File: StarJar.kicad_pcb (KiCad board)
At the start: 2 copper layers, 127 x 50.8 mm, 38 parts, among them J1 USB_A, J2 GM_Tube, J3 Screw_Terminal_1x02, Q1 JN3303, Q2 2N3904, Q3 2N3904, Q4 2N3904, U1 LM555N, U2 LMV321

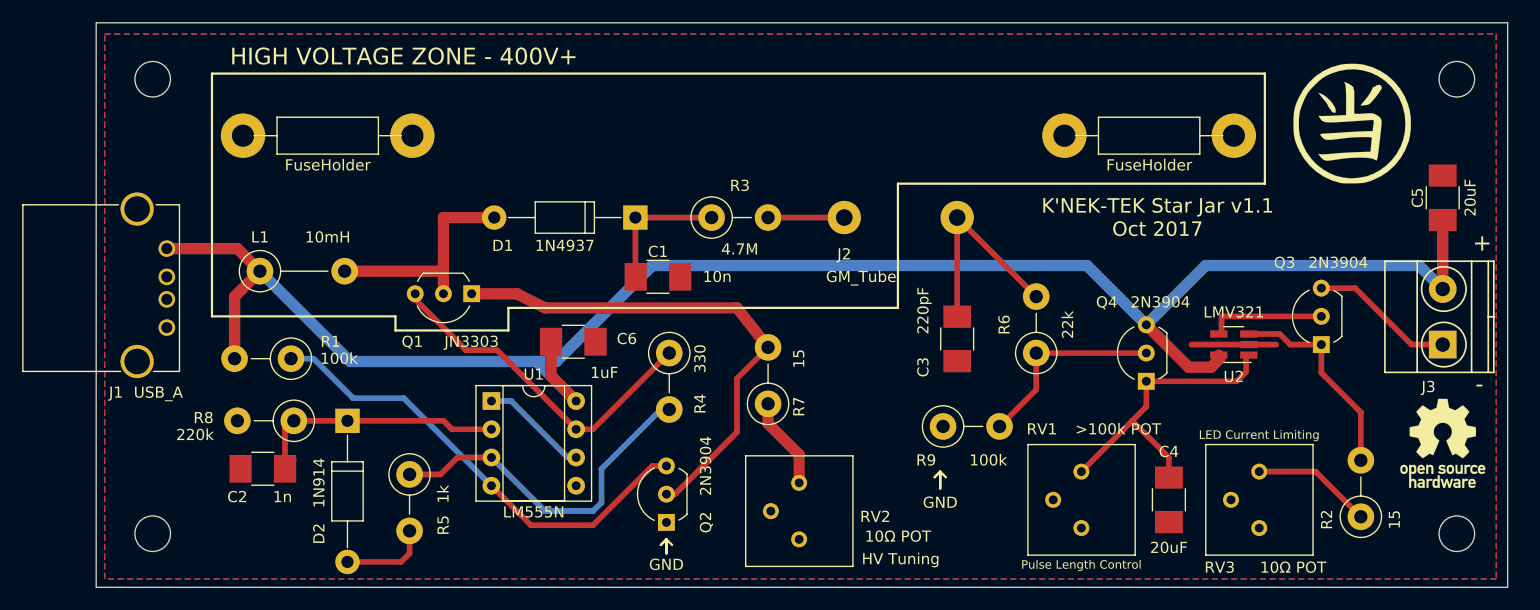
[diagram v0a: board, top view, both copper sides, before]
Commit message: Add files via upload
v1.2 board layout finished, ready to order. Changes: zip tie mounts for GM tube, USB micro-B rather than USB-A, added new components to fix pulse size issue.
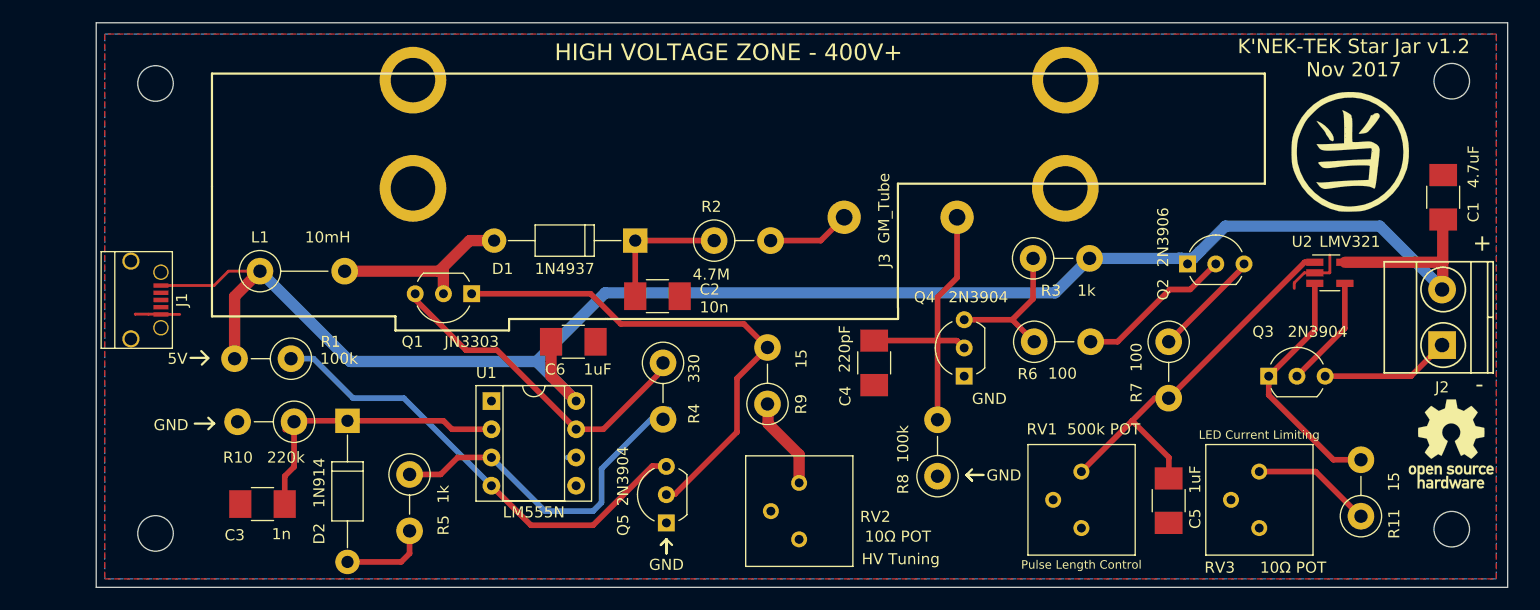
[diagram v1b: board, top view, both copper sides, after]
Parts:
- removed the FuseHolder1 at (149.4, 64.8)
- removed the FuseHolder1 at (75.4, 64.8)
- removed the REF** at (184.7, 59.7)
- removed the REF** at (184.7, 100.6)
- removed the REF** at (67.3, 100.6)
- removed the REF** at (67.3, 59.7)
- added FuseHolder1: ZipTie, CustomFootprints:GM_tube_ziptie_mounts, F.Cu at (90.7, 69.5)
- added FuseHolder1: ZipTie, CustomFootprints:GM_tube_ziptie_mounts, F.Cu at (149.4, 69.5)
- added Q5: 2N3904, TO_SOT_Packages_THT:TO-92_Inline_Wide, F.Cu at (113.5, 99.6)
- added R10: 220k, Resistors_THT:R_Axial_DIN0411_L9.9mm_D3.6mm_P5.08mm_Vertical, F.Cu at (80.0, 90.5)
- added R11: 15, Resistors_THT:R_Axial_DIN0411_L9.9mm_D3.6mm_P5.08mm_Vertical, F.Cu at (176.0, 99.0)
- added REF**: MountingHole_3.2mm_M3, Mounting_Holes:MountingHole_3.2mm_M3, F.Cu at (184.2, 100.2)
- added REF**: MountingHole_3.2mm_M3, Mounting_Holes:MountingHole_3.2mm_M3, F.Cu at (184.2, 59.9)
- added REF**: MountingHole_3.2mm_M3, Mounting_Holes:MountingHole_3.2mm_M3, F.Cu at (67.6, 100.6)
- added REF**: MountingHole_3.2mm_M3, Mounting_Holes:MountingHole_3.2mm_M3, F.Cu at (67.6, 60.1)
- C1: value 10n -> 4.7uF
- C2: value 1n -> 10n
- C3: value 220pF -> 1n
- C4: value 20uF -> 220pF
- C5: value 20uF -> 1uF
- J1: value USB_A -> USB_OTG; footprint Connectors:USB_A -> CustomFootprints:USB_Micro-B_big_holes_for_OSHpark
- J2: value GM_Tube -> Screw_Terminal_1x02; footprint Wire_Connections_Bridges:WireConnection_1.50mmDrill -> Connectors_Terminal_Blocks:TerminalBlock_Pheonix_MKDS1.5-2pol
- J3: value Screw_Terminal_1x02 -> GM_Tube; footprint Connectors_Terminal_Blocks:TerminalBlock_Pheonix_MKDS1.5-2pol -> Wire_Connections_Bridges:WireConnection_1.50mmDrill
- Q2: value 2N3904 -> 2N3906
- R2: value 15 -> 4.7M
- R3: value 4.7M -> 1k
- R6: value 22k -> 100
- R7: value 15 -> 100
- R8: value 220k -> 100k
- R9: value 100k -> 15
- RV1: value >100k POT -> 500k POT
- moved C1 71.0 mm to (183.4, 70.3), turned to 90 degrees
- moved C3 64.3 mm to (77.2, 97.9), turned to 180 degrees
- moved R2 63.3 mm to (117.8, 74.2), turned to 0 degrees
- moved R8 58.1 mm to (137.9, 95.4), turned to 90 degrees
- moved J3 55.1 mm to (129.5, 72.1), turned to 0 degrees
- moved J2 55.0 mm to (183.3, 83.6), turned to 90 degrees
- moved Q2 52.3 mm to (160.4, 76.3), turned to 0 degrees
- moved C2 38.8 mm to (112.7, 79.2), turned to 0 degrees
- moved C5 36.8 mm to (158.7, 97.6), turned to 270 degrees
- moved R7 36.5 mm to (158.7, 83.3), turned to 270 degrees
- moved C4 29.2 mm to (132.2, 85.2)
- moved R3 29.2 mm to (146.5, 75.8)
- moved Q4 16.4 mm to (140.3, 86.4)
- moved R9 15.9 mm to (122.6, 88.9), turned to 90 degrees
- moved U2 10.8 mm to (173.2, 77.1), turned to 0 degrees
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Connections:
- C1 pad 1: Net-(C1-Pad1) -> +5V
- C4 pad 1: /PulseOutput -> Net-(C4-Pad1)
- C5 pad 1: +5V -> /PulseOutput
- D1 pad 1: Net-(C1-Pad1) -> Net-(C2-Pad1)
- D2 pad 1: Net-(C2-Pad1) -> Net-(C3-Pad1)
- J1 pad 2: Net-(J1-Pad2) -> (no net)
- J1 pad 3: Net-(J1-Pad3) -> (no net)
- J1 pad 4: GND -> (no net)
- J2 pad 2: Net-(C3-Pad1) -> +5V
- J3 pad 2: +5V -> Net-(C4-Pad1)
- Q2 pad 1: GND -> +5V
- Q2 pad 2: Net-(Q1-Pad1) -> Net-(Q2-Pad2)
- Q3 pad 3: Net-(J3-Pad1) -> Net-(J2-Pad1)
- Q4 pad 1: /PulseOutput -> GND
- Q4 pad 2: Net-(Q4-Pad2) -> Net-(C4-Pad1)
- Q4 pad 3: +5V -> Net-(Q4-Pad3)
- R1 pad 1: Net-(Q2-Pad3) -> Net-(Q5-Pad3)
- R2 pad 1: Net-(R2-Pad1) -> Net-(C2-Pad1)
- R2 pad 2: Net-(Q3-Pad1) -> Net-(J3-Pad1)
- R3 pad 1: Net-(C1-Pad1) -> Net-(Q4-Pad3)
- R3 pad 2: Net-(J2-Pad1) -> +5V
- R6 pad 1: Net-(Q4-Pad2) -> Net-(Q4-Pad3)
- R6 pad 2: Net-(C3-Pad1) -> Net-(Q2-Pad2)
- R7 pad 1: Net-(R7-Pad1) -> Net-(Q2-Pad3)
- R7 pad 2: Net-(Q1-Pad1) -> /PulseOutput
- R8 pad 1: Net-(C2-Pad1) -> GND
- R8 pad 2: GND -> Net-(C4-Pad1)
- R9 pad 1: GND -> Net-(R9-Pad1)
- R9 pad 2: Net-(Q4-Pad2) -> Net-(Q1-Pad1)
- RV1 pad 3: Net-(RV1-Pad3) -> (no net)
- RV2 pad 1: Net-(R7-Pad1) -> Net-(R9-Pad1)
- RV2 pad 3: Net-(RV2-Pad3) -> (no net)
- RV3 pad 1: Net-(R2-Pad1) -> Net-(R11-Pad1)
- RV3 pad 3: Net-(RV3-Pad3) -> (no net)
- U1 pad 2: Net-(C2-Pad1) -> Net-(C3-Pad1)
- U1 pad 4: Net-(Q2-Pad3) -> Net-(Q5-Pad3)
- U1 pad 5: Net-(U1-Pad5) -> (no net)
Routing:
- net Net-(Q5-Pad3): track 0.00 -> 42.2 mm
- net Net-(Q2-Pad3): track 42.2 -> 9.81 mm
- net Net-(C4-Pad1): track 0.00 -> 27.3 mm
- net Net-(Q4-Pad2): track 17.9 -> 0.00 mm
- net Net-(Q2-Pad2): track 0.00 -> 14.2 mm
- net Net-(Q4-Pad3): track 0.00 -> 13.4 mm
- net Net-(C1-Pad1): track 12.7 -> 0.00 mm
- net Net-(C2-Pad1): track 23.9 -> 12.1 mm
- net Net-(R2-Pad1): track 10.8 -> 0.00 mm
- net Net-(R11-Pad1): track 0.00 -> 10.8 mm
- net Net-(R9-Pad1): track 0.00 -> 8.27 mm
- net Net-(R7-Pad1): track 8.27 -> 0.00 mm
- net Net-(C3-Pad1): track 19.0 -> 27.0 mm
- net /PulseOutput: track 27.9 -> 35.3 mm
- net GND: track 17.3 -> 10.6 mm
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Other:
- board text added: "1.2"
- board text added: "5V"
- board text added: "Design files available at: https://github.com/Erik-k/StarJar"
- board text added: "K'NEK-TEK Star Jar v1.2 Nov 2017"
- board text removed: "1.1"
- board text removed: "K'NEK-TEK Star Jar v1.1 Oct 2017"

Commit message: Add files via upload
Minor changes to PCB silkscreen. Ordered the boards.
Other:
- board text added: "November 2017"
- board text removed: "1.0"
- board text removed: "September 2017"
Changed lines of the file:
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@@
-(kicad_pcb (version 4) (host pcbnew 4.0.6)
+(kicad_pcb (version 4) (host pcbnew 4.0.7)
   (general
     (links 62)
     (no_connects 0)
-    (area 62.179999 54.559999 189.280001 105.460001)
+    (area 57.952857 54.559999 255.277714 200.486)
     (thickness 1.6)
-    (drawings 61)
+    (drawings 60)
     (tracks 132)
     (zones 0)
@@
     (45 Margin user)
     (47 F.CrtYd user)
-    (49 F.Fab user hide)
+    (49 F.Fab user)
   )
   (setup
@@
     (descr "D, DO-41_SOD81 series, Axial, Horizontal, pin pitch=12.7mm, , length*diameter=5.2*2.7mm^2, , http://www.diodes.com/_files/packages/DO-41%20(Plastic).pdf")
     (tags "D DO-41_SOD81 series Axial Horizontal pin pitch 12.7mm  length 5.2mm diameter 2.7mm")
-    (fp_text reference D1 (at 11.938 -2.54 180) (layer F.SilkS)
-      (effects (font (size 1 1) (thickness 0.15)))
-    )
-    (fp_text value 1N4937 (at 6.35 -2.54 180) (layer F.SilkS)
+    (fp_text reference D1 (at 9.1046 -2.5742 180) (layer F.SilkS)
+      (effects (font (size 1 1) (thickness 0.15)))
+    )
+    (fp_text value 1N4937 (at 4.1008 -2.54 180) (layer F.SilkS)
       (effects (font (size 1 1) (thickness 0.15)))
     )
@@
     (descr "TO-92 leads in-line, wide, drill 0.8mm (see NXP sot054_po.pdf)")
     (tags "to-92 sc-43 sc-43a sot54 PA33 transistor")
-    (fp_text reference Q1 (at 5.334 -4.318 360) (layer F.SilkS)
-      (effects (font (size 1 1) (thickness 0.15)))
-    )
-    (fp_text value JN3303 (at 0 -4.318 180) (layer F.SilkS)
+    (fp_text reference Q1 (at -2.5908 0.381 360) (layer F.SilkS)
+      (effects (font (size 1 1) (thickness 0.15)))
+    )
+    (fp_text value JN3303 (at -4.318 -1.2954 180) (layer F.SilkS)
       (effects (font (size 1 1) (thickness 0.15)))
     )
@@
       (effects (font (size 1 1) (thickness 0.15)))
     )
-    (fp_text value 4.7M (at -0.254 3.048) (layer F.SilkS)
+    (fp_text value 4.7M (at 4.2932 -2.9884) (layer F.SilkS)
       (effects (font (size 1 1) (thickness 0.15)))
     )
@@
   (gr_line (start 72.3138 84.7852) (end 71.7296 85.3694) (angle 90) (layer F.SilkS) (width 0.2))
   (gr_line (start 72.3138 84.7852) (end 71.6788 84.1502) (angle 90) (layer F.SilkS) (width 0.2))
-  (gr_text 5V (at 69.5452 84.836) (layer F.SilkS)
+  (gr_text 5V (at 71.7296 83.2866) (layer F.SilkS)
     (effects (font (size 1 1) (thickness 0.15)))
   )
@@
   (gr_text "LED Current Limiting" (at 166.878 91.694) (layer F.SilkS)
     (effects (font (size 0.762 0.762) (thickness 0.127)))
-  )
-  (gr_text 1.2 (at 252.476 199.136) (layer Dwgs.User)
-    (effects (font (size 1.5 1.5) (thickness 0.3)))
   )
   (gr_line (start 113.538 101.092) (end 114.046 101.6) (angle 90) (layer F.SilkS) (width 0.2))
@@
     (effects (font (size 1.5 1.5) (thickness 0.3)))
   )
-  (gr_text 1.0 (at 253.492 198.882) (layer F.Fab)
+  (gr_text 1.2 (at 253.492 198.882) (layer F.Fab)
     (effects (font (size 1.5 1.5) (thickness 0.3)))
   )
-  (gr_text "September 2017" (at 200.152 198.882) (layer F.Fab)
+  (gr_text "November 2017" (at 200.152 198.882) (layer F.Fab)
     (effects (font (size 1.5 1.5) (thickness 0.3)))
   )
